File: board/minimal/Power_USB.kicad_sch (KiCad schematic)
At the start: 11 parts, among them J2 USB_C_Receptacle_USB2.0_14P, U4 STUSB4500QTR

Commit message: update PCB and edit schematic
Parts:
- removed J2: USB_C_Receptacle_USB2.0_14P, symbol Connector:USB_C_Receptacle_USB2.0_14P
- added J17: 5077CR-16SMC2-BK-TR, NELTRON_5077CR-16SMC2-BK-TR, symbol 5077CR-16SMC2-BK-TR:5077CR-16SMC2-BK-TR
- C19, C20: footprint (none) -> Capacitor_SMD:C_0603_1608Metric
- D1, D2: footprint (none) -> LED_SMD:LED_0603_1608Metric
- R10, R6, R7, R8, R9: footprint (none) -> Resistor_SMD:R_0603_1608Metric
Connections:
- net D+: now also J17.A6 (DP1), J17.B6 (DP2)
- net D-: now also J17.A7 (DN1), J17.B7 (DN2)
- net GND: now also J17.A1_B12 (GND), J17.B1_A12 (GND), J17.S1 (SHIELD), J17.S2 (SHIELD), J17.S3 (SHIELD), J17.S4 (SHIELD)
- net VBUS: now also J17.A4_B9 (VBUS), J17.B4_A9 (VBUS)
- net CC1: now reaches U4.1 (CC1DB), U4.2 (CC1)
- net CC1: now also J17.A5 (CC1)
- net CC2: now reaches U4.4 (CC2), U4.5 (CC2DB)
- net CC2: now also J17.B5 (CC2)
- no-connect marks 4 -> 6
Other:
- moved on the sheet: C19, C20, D1, D2, R10, R6, R7, R8, R9, U4

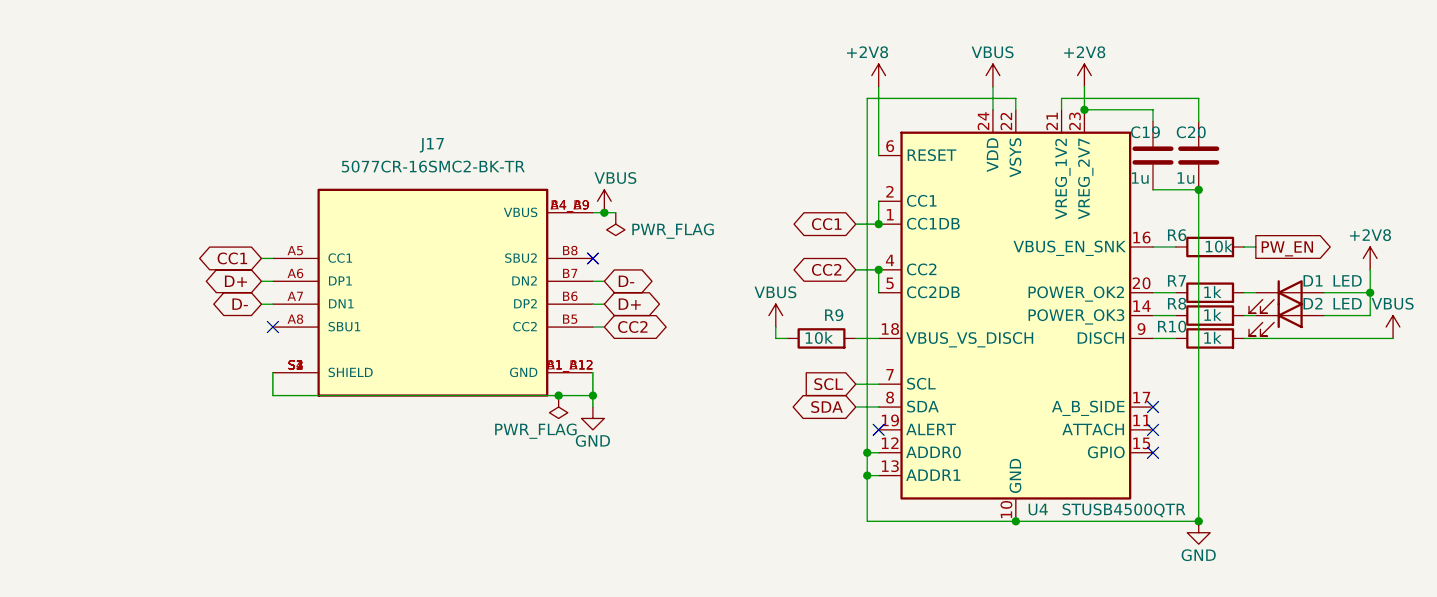
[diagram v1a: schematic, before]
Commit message: add Weather to Dashboard
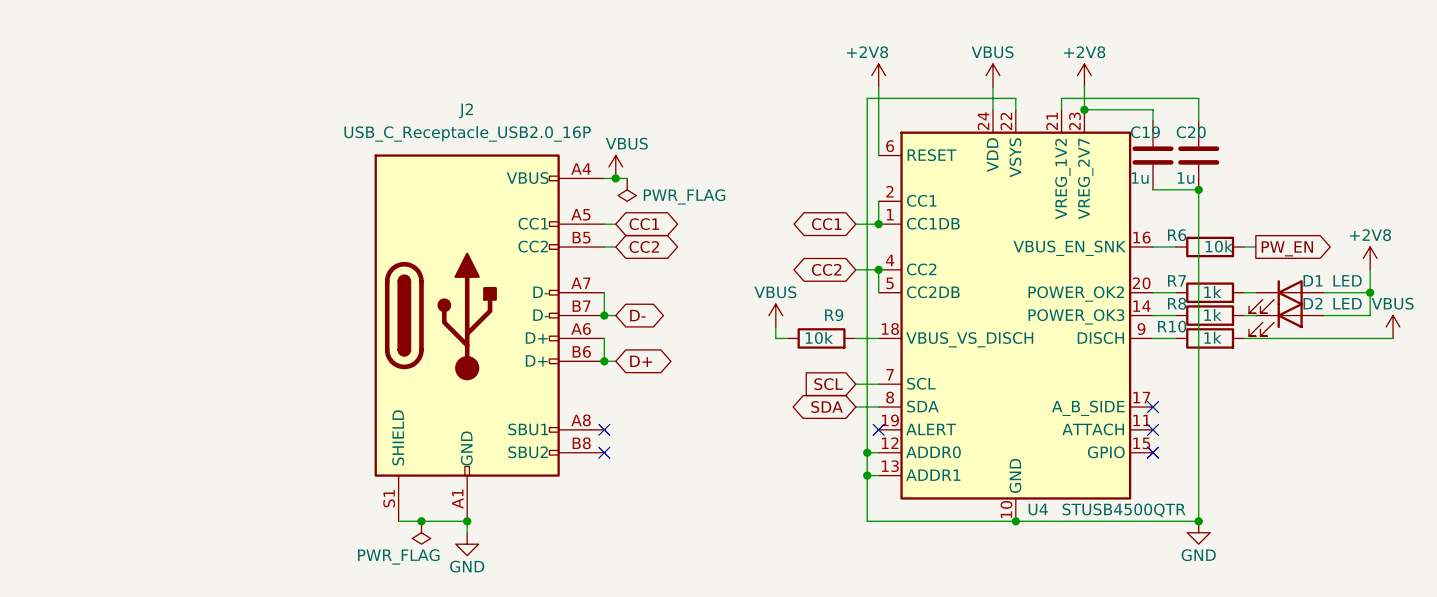
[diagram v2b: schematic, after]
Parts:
- removed J17: 5077CR-16SMC2-BK-TR, NELTRON_5077CR-16SMC2-BK-TR, symbol 5077CR-16SMC2-BK-TR:5077CR-16SMC2-BK-TR
- added J2: USB_C_Receptacle_USB2.0_16P, Connector_USB:USB_C_Receptacle_GCT_USB4085, symbol Connector:USB_C_Receptacle_USB2.0_16P
- C19, C20: footprint Capacitor_SMD:C_0603_1608Metric -> Capacitor_SMD:C_0201_0603Metric
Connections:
- net CC1: now also J2.A5 (CC1)
- net CC2: now also J2.B5 (CC2)
- net D+: now also J2.A6 (D+), J2.B6 (D+)
- net D-: now also J2.A7 (D-), J2.B7 (D-)
- net GND: now also J2.A1 (GND), J2.A12 (GND), J2.B1 (GND), J2.B12 (GND), J2.S1 (SHIELD)
- net VBUS: now also J2.A4 (VBUS), J2.A9 (VBUS), J2.B4 (VBUS), J2.B9 (VBUS)
